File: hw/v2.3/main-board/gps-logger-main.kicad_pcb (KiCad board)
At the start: 4 copper layers, 40.9 x 72.7 mm, 84 parts, among them J1 gnss-conn, J2 tag-connect, J3 USB_C_Receptacle, J4 Conn_01x03_MountingPin, Q1 AP3400, Q2 AP3401, Q3 AP3401, Q4 AP3401, SW1 SW_Push, U1 MSP430F5514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

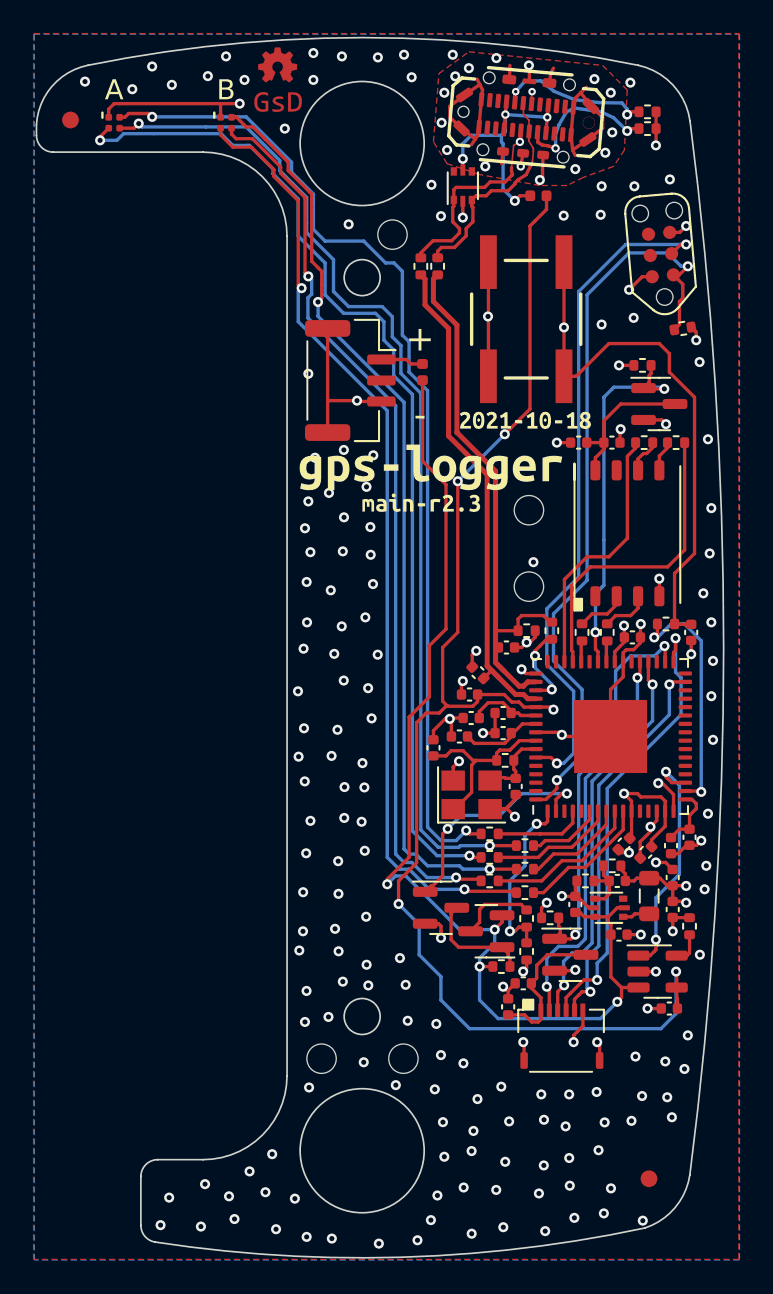
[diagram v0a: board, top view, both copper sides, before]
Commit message: Update r2.3
- Add make panel KiKit script
- Add production gerbers
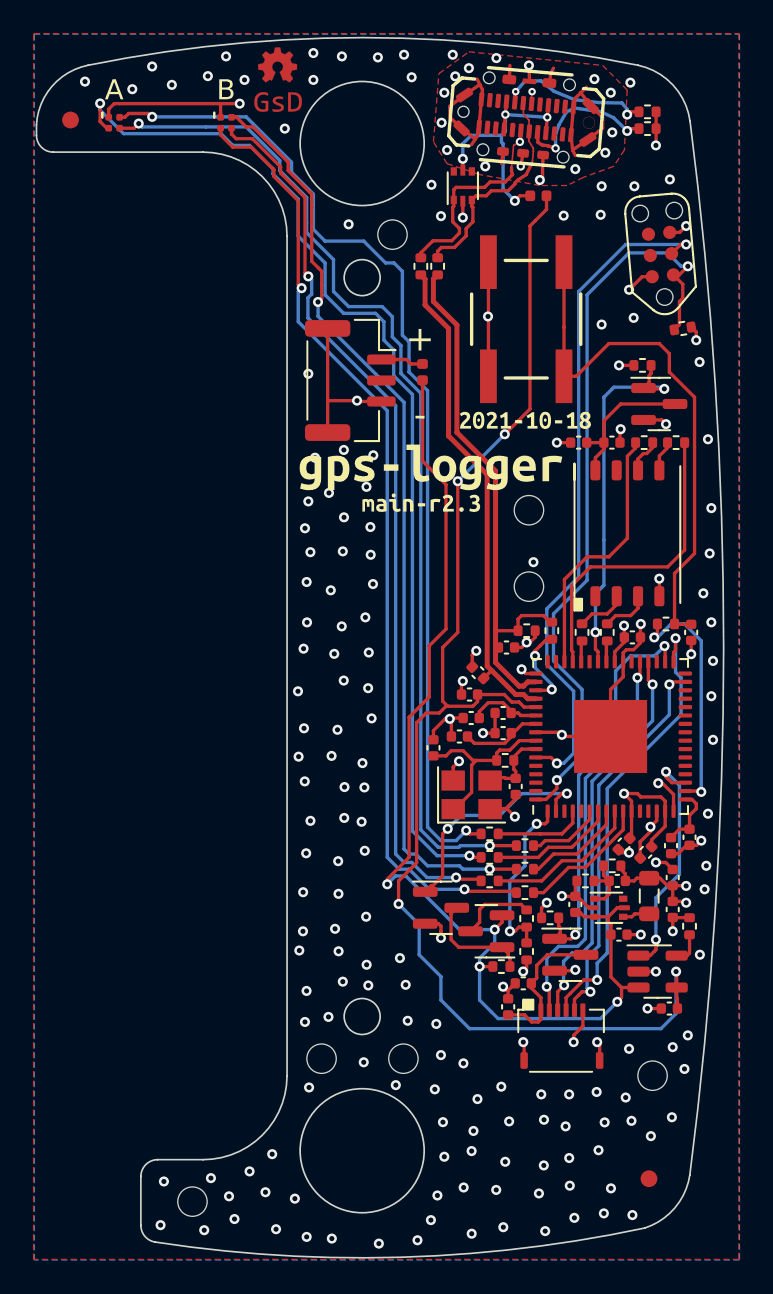
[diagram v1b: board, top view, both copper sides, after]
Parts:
- added REF**: M1.6_Mounting Hole, gps-logger:M1.6_Mounting Hole, F.Cu at (168.8, 128.0)
- added REF**: M1.6_Mounting Hole, gps-logger:M1.6_Mounting Hole, F.Cu at (141.4, 135.5)
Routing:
- net Net-(D1-Pad2): track 61.0 -> 62.6 mm
- net GND: track 102.4 -> 100.8 mm
- net pp-vbus: track 80.5 -> 79.3 mm, vias 5 -> 4
- net /MSP430/msp-usb-data-: track 30.3 -> 29.3 mm
- net /MSP430/msp-usb-data+: track 33.0 -> 32.2 mm
- net Net-(C17-Pad2): vias 1 -> 0

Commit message: Update PCBs to remove small vias
- Regenerate 1x panel
- Add gerbers
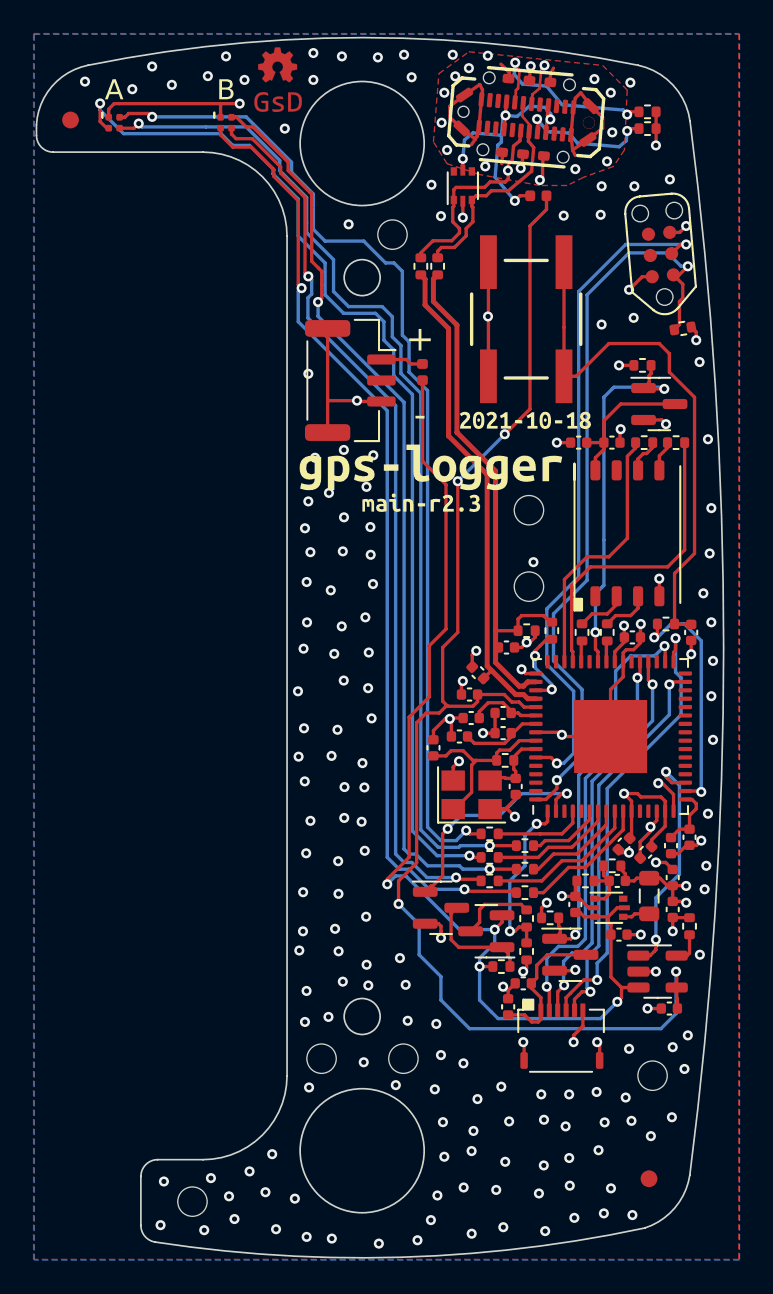
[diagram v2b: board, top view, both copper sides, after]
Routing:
- net usb-d-: track 16.5 -> 22.2 mm
- net Net-(J3-PadA5): track 9.16 -> 11.6 mm
- net Net-(F1-Pad1): track 16.5 -> 17.8 mm
- net Net-(J3-PadB5): track 9.01 -> 8.25 mm
